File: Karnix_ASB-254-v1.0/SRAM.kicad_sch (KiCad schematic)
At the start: 4 parts, among them U21 K6R4016V1D-TC10 (TSOP-44, +3.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

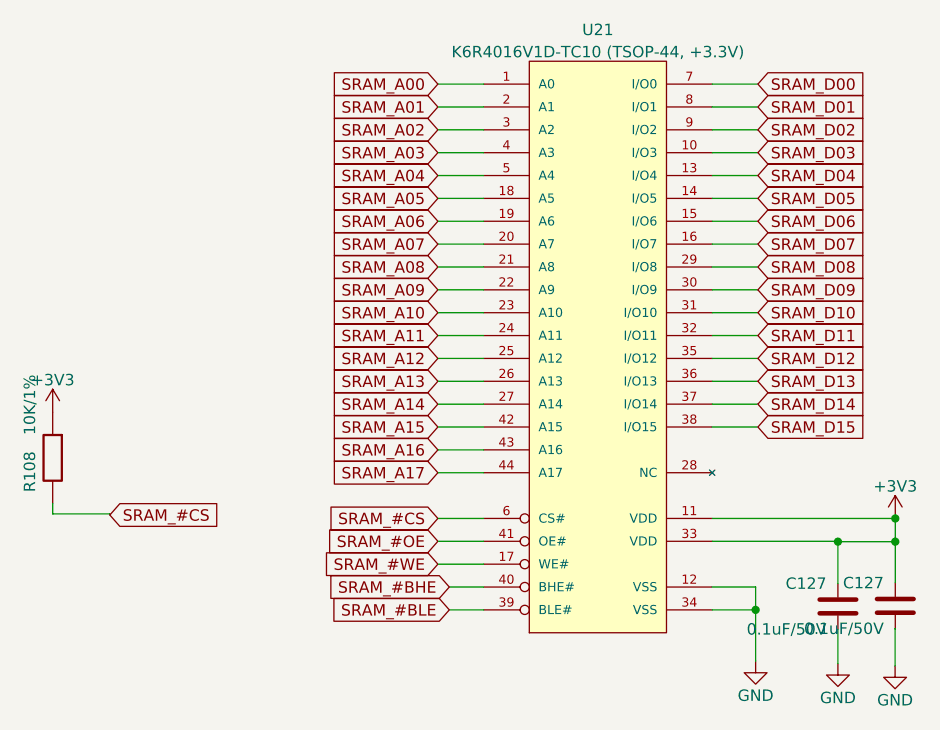
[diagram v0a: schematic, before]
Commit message: Remove rudimentary referencies to old projects
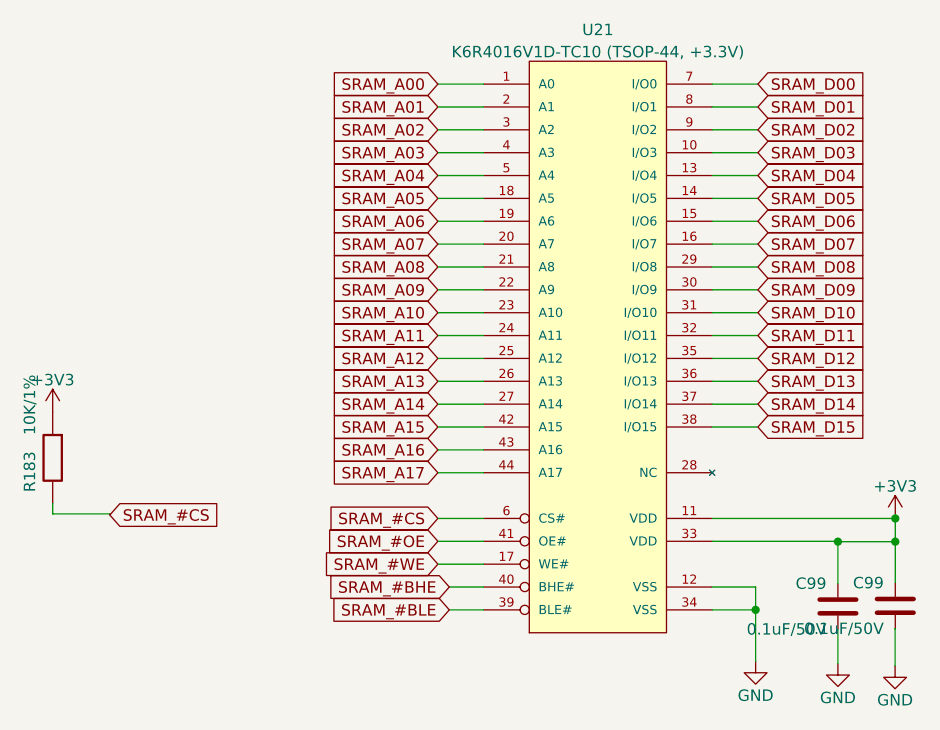
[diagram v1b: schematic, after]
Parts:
- renumbered C127 to C99, R108 to R183
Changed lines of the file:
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@@
   (symbol (lib_id "power:GND") (at 215.773 156.845 0) (unit 1)
     (in_bom yes) (on_board yes) (dnp no)
-    (property "Reference" "#PWR0218" (at 215.773 163.195 0)
+    (property "Reference" "#PWR0251" (at 215.773 163.195 0)
       (effects (font (size 1.27 1.27)) hide)
     )
@@
     (pin "1")
     (instances
-      (project "SIP_HomePhone"
-        (path "/1f1efc58-1a2e-4658-b2ac-cf03134c8a7b/00000000-0000-0000-0000-00005ddd7833"
-          (reference "#PWR0218") (unit 1)
-        )
-      )
       (project "Karnix_ASB"
         (path "/fe37e245-9527-4c72-91fc-09b617a42f73/af986742-b82e-4f48-bf7e-cdfbb60b3231"
@@
   (symbol (lib_id "power:GND") (at 200.279 156.337 0) (unit 1)
     (in_bom yes) (on_board yes) (dnp no)
-    (property "Reference" "#PWR0218" (at 200.279 162.687 0)
+    (property "Reference" "#PWR0251" (at 200.279 162.687 0)
       (effects (font (size 1.27 1.27)) hide)
     )
@@
     (pin "1")
     (instances
-      (project "SIP_HomePhone"
-        (path "/1f1efc58-1a2e-4658-b2ac-cf03134c8a7b/00000000-0000-0000-0000-00005ddd7833"
-          (reference "#PWR0218") (unit 1)
-        )
-      )
       (project "Karnix_ASB"
         (path "/fe37e245-9527-4c72-91fc-09b617a42f73/af986742-b82e-4f48-bf7e-cdfbb60b3231"
@@
   (symbol (lib_id "Fabmicro:CapacitorUnpolarized") (at 209.423 150.241 90) (mirror x) (unit 1)
     (in_bom yes) (on_board yes) (dnp no)
-    (property "Reference" "C127" (at 208.153 147.701 90)
+    (property "Reference" "C99" (at 208.153 147.701 90)
       (effects (font (size 1.27 1.27)) (justify left))
     )
@@
     (pin "2")
     (instances
-      (project "SIP_HomePhone"
-        (path "/1f1efc58-1a2e-4658-b2ac-cf03134c8a7b/00000000-0000-0000-0000-00005ddd7833"
-          (reference "C127") (unit 1)
-        )
-      )
       (project "Karnix_ASB"
         (path "/fe37e245-9527-4c72-91fc-09b617a42f73/af986742-b82e-4f48-bf7e-cdfbb60b3231"
@@
   (symbol (lib_id "Fabmicro:CapacitorUnpolarized") (at 215.7962 150.1748 90) (mirror x) (unit 1)
     (in_bom yes) (on_board yes) (dnp no)
-    (property "Reference" "C127" (at 214.5262 147.6348 90)
+    (property "Reference" "C99" (at 214.5262 147.6348 90)
       (effects (font (size 1.27 1.27)) (justify left))
     )
@@
     (pin "2")
     (instances
-      (project "SIP_HomePhone"
-        (path "/1f1efc58-1a2e-4658-b2ac-cf03134c8a7b/00000000-0000-0000-0000-00005ddd7833"
-          (reference "C127") (unit 1)
-        )
-      )
       (project "Karnix_ASB"
         (path "/fe37e245-9527-4c72-91fc-09b617a42f73/af986742-b82e-4f48-bf7e-cdfbb60b3231"
@@
   (symbol (lib_id "power:GND") (at 209.423 156.591 0) (unit 1)
     (in_bom yes) (on_board yes) (dnp no)
-    (property "Reference" "#PWR0218" (at 209.423 162.941 0)
+    (property "Reference" "#PWR0251" (at 209.423 162.941 0)
       (effects (font (size 1.27 1.27)) hide)
     )
@@
     (pin "1")
     (instances
-      (project "SIP_HomePhone"
-        (path "/1f1efc58-1a2e-4658-b2ac-cf03134c8a7b/00000000-0000-0000-0000-00005ddd7833"
-          (reference "#PWR0218") (unit 1)
-        )
-      )
       (project "Karnix_ASB"
         (path "/fe37e245-9527-4c72-91fc-09b617a42f73/af986742-b82e-4f48-bf7e-cdfbb60b3231"
@@
   (symbol (lib_id "Fabmicro:Resistor") (at 122.174 133.731 90) (unit 1)
     (in_bom yes) (on_board yes) (dnp no)
-    (property "Reference" "R108" (at 119.634 137.541 0)
+    (property "Reference" "R183" (at 119.634 137.541 0)
       (effects (font (size 1.27 1.27)) (justify left))
     )
@@
     (pin "2")
     (instances
-      (project "SIP_HomePhone"
-        (path "/1f1efc58-1a2e-4658-b2ac-cf03134c8a7b/00000000-0000-0000-0000-00005ddd7833"
-          (reference "R108") (unit 1)
-        )
-      )
-      (project "Karnix_ASB"
-        (path "/fe37e245-9527-4c72-91fc-09b617a42f73/af986742-b82e-4f48-bf7e-cdfbb60b3231"
+      (project "Karnix_ASB"
+        (path "/fe37e245-9527-4c72-91fc-09b617a42f73/af986742-b82e-4f48-bf7e-cdfbb60b3231"
